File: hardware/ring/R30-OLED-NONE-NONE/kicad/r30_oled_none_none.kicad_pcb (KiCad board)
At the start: 2 copper layers, 42 x 18 mm, 32 parts, among them J1 USB4215-class 16P TH stakes, Q1 SI2301 P-FET, Q2 2N7002 gate driver, SW1 5mm 200gf dome, U1 ESP32-C3-MINI-1-N4, U2 PAW3204DB-TJ3L, U3 TP4054, U4 RT9080-33GJ5

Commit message: fix(r30): move dome away from mcu pad column
Sensing mechanism: PAW3204 optical surface tracking.

Form factor and angle: R30 30-degree ring, OLED/NONE/NONE active lane.

Intended use: accessibility-first BLE HID pointing first-board validation.

BOM estimate: active R30 prototype remains about $5.30-$9.45, target about $9.
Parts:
- moved SW1 2.41 mm to (114.2, 95.0)
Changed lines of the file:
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@@
   (footprint "PowerFinger_Ring:Snap_Dome_5mm_TwoPad_Serviceable"
     (layer "F.Cu")
-    (at 116.550 94.450 0)
+    (at 114.200 95.000 0)
     (descr "5 mm metal snap dome contacts; accessible click zone")
     (property "Reference" "SW1" (at 0 -3.05 0) (layer "F.SilkS") (effects (font (size 0.75 0.75) (thickness 0.11))))
@@
   (segment (start 119.300 99.365) (end 122.050 97.900) (width 0.20) (layer "F.Cu") (net 13))
   (segment (start 119.300 98.095) (end 122.050 96.000) (width 0.20) (layer "F.Cu") (net 14))
-  (segment (start 117.750 103.000) (end 116.550 94.450) (width 0.20) (layer "F.Cu") (net 15))
+  (segment (start 117.750 103.000) (end 114.200 95.000) (width 0.20) (layer "F.Cu") (net 15))
   (segment (start 105.500 99.500) (end 108.350 105.050) (width 0.20) (layer "F.Cu") (net 16))
   (segment (start 108.350 106.950) (end 120.800 106.350) (width 0.20) (layer "F.Cu") (net 16))

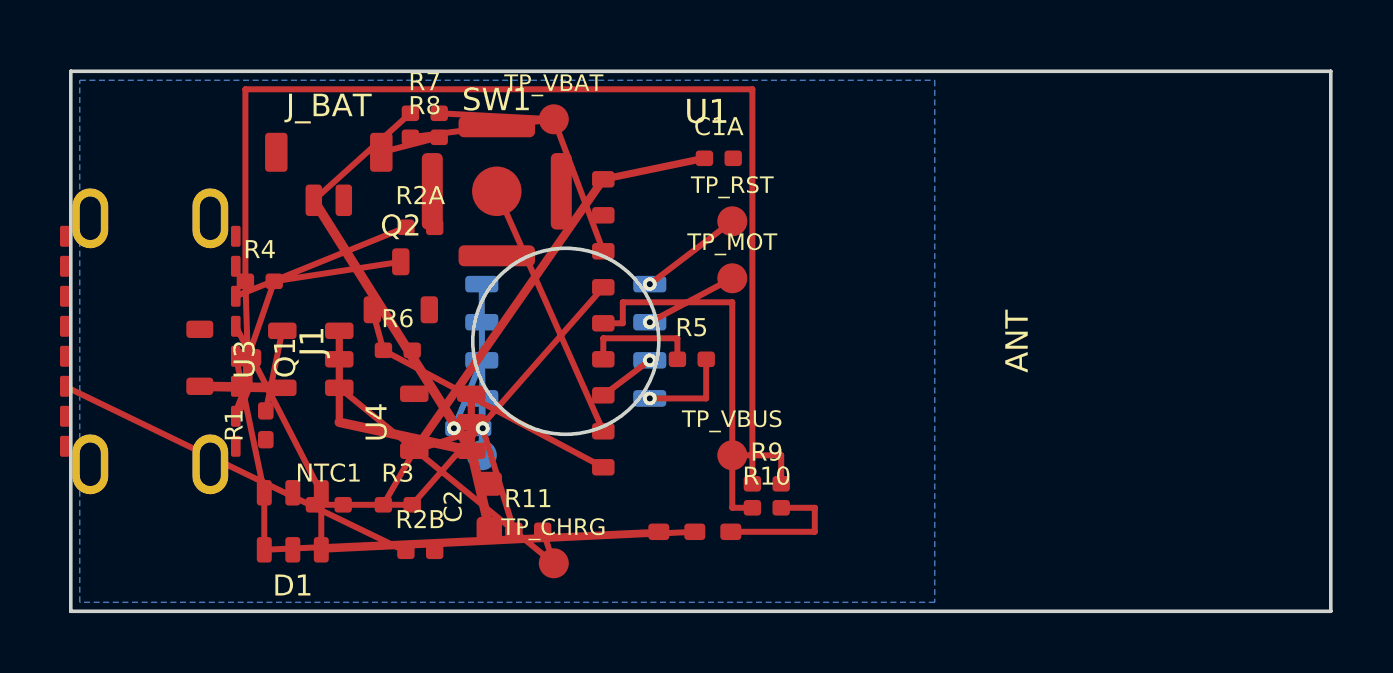
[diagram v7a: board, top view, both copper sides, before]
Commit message: fix(r30): correct charge service endpoints
Sensing mechanism: PAW3204 optical surface tracking.

Form factor and angle: R30 30-degree ring, OLED/NONE/NONE active lane.

Intended use: accessibility-first BLE HID pointing first-board validation.

BOM estimate: active R30 prototype remains about $5.30-$9.45, target about $9.
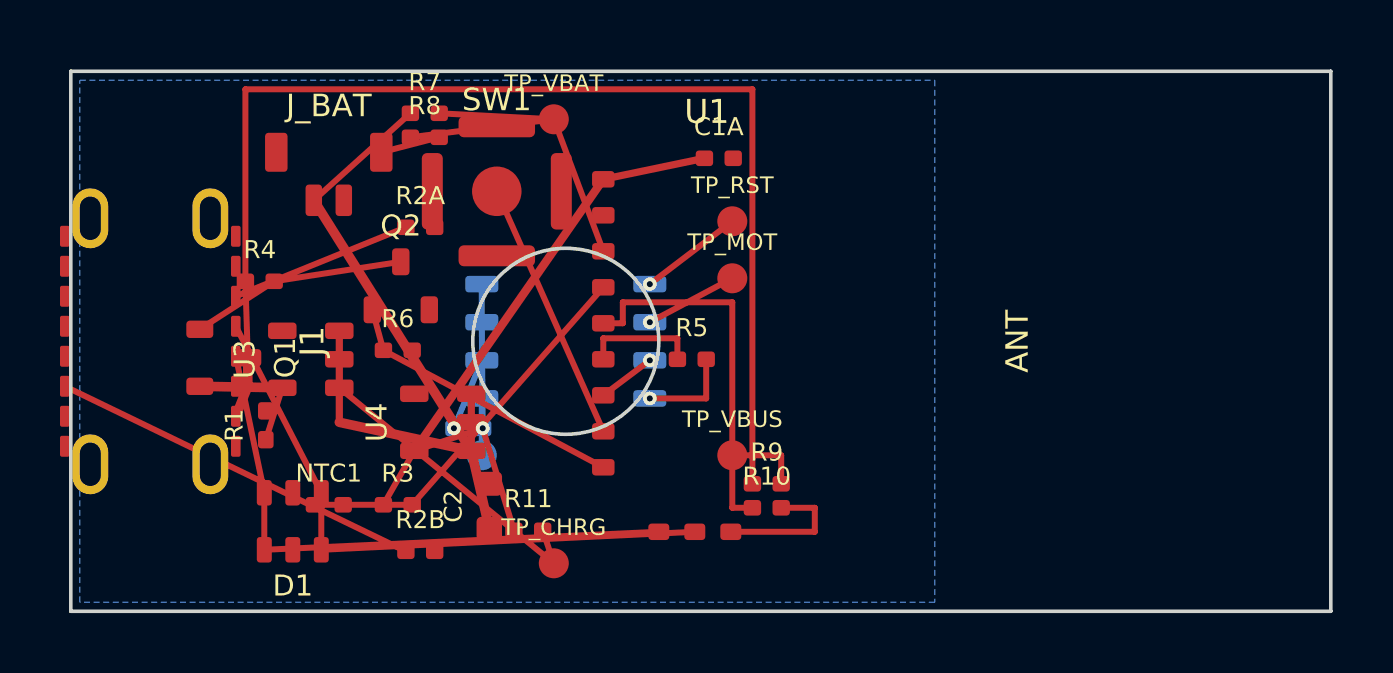
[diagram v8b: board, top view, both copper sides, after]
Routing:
- net PROG_R: track 2.73 -> 1.82 mm
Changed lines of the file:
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@@
   (segment (start 113.700 99.365) (end 113.700 98.095) (width 0.20) (layer "B.Cu") (net 5))
   (segment (start 112.770 102.900) (end 113.700 100.635) (width 0.20) (layer "B.Cu") (net 1))
-  (segment (start 107.050 99.650) (end 106.500 102.320) (width 0.20) (layer "F.Cu") (net 6))
-  (segment (start 105.900 100.550) (end 106.780 98.000) (width 0.20) (layer "F.Cu") (net 7))
+  (segment (start 107.050 101.550) (end 106.500 103.280) (width 0.20) (layer "F.Cu") (net 6))
+  (segment (start 104.300 99.600) (end 106.780 98.000) (width 0.20) (layer "F.Cu") (net 7))
   (segment (start 106.780 98.000) (end 111.000 97.350) (width 0.20) (layer "F.Cu") (net 7))
   (segment (start 110.050 98.950) (end 110.420 100.300) (width 0.20) (layer "F.Cu") (net 8))
